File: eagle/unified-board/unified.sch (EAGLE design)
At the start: 78 parts, among them IC101 THAT151x, J103 phantom, J104 eqout, J601 out2, U101 OPAMPLME49710, U602 LM3915N, U603 OPAMPLME49710

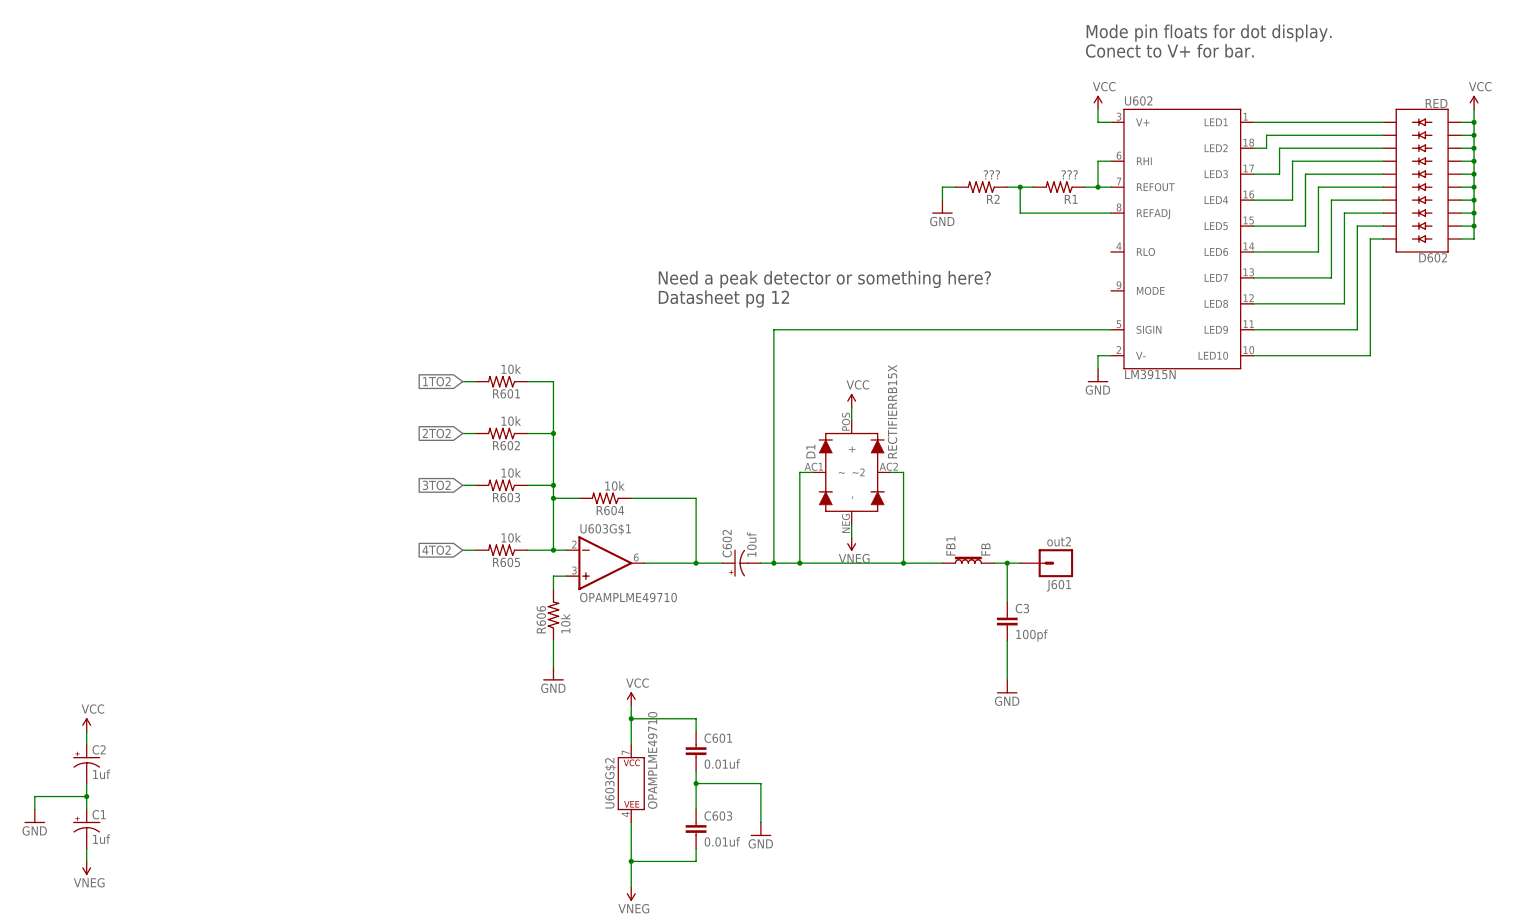
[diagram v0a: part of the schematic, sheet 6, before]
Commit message: Some initial routing
one input, one output, placeholders  for more.
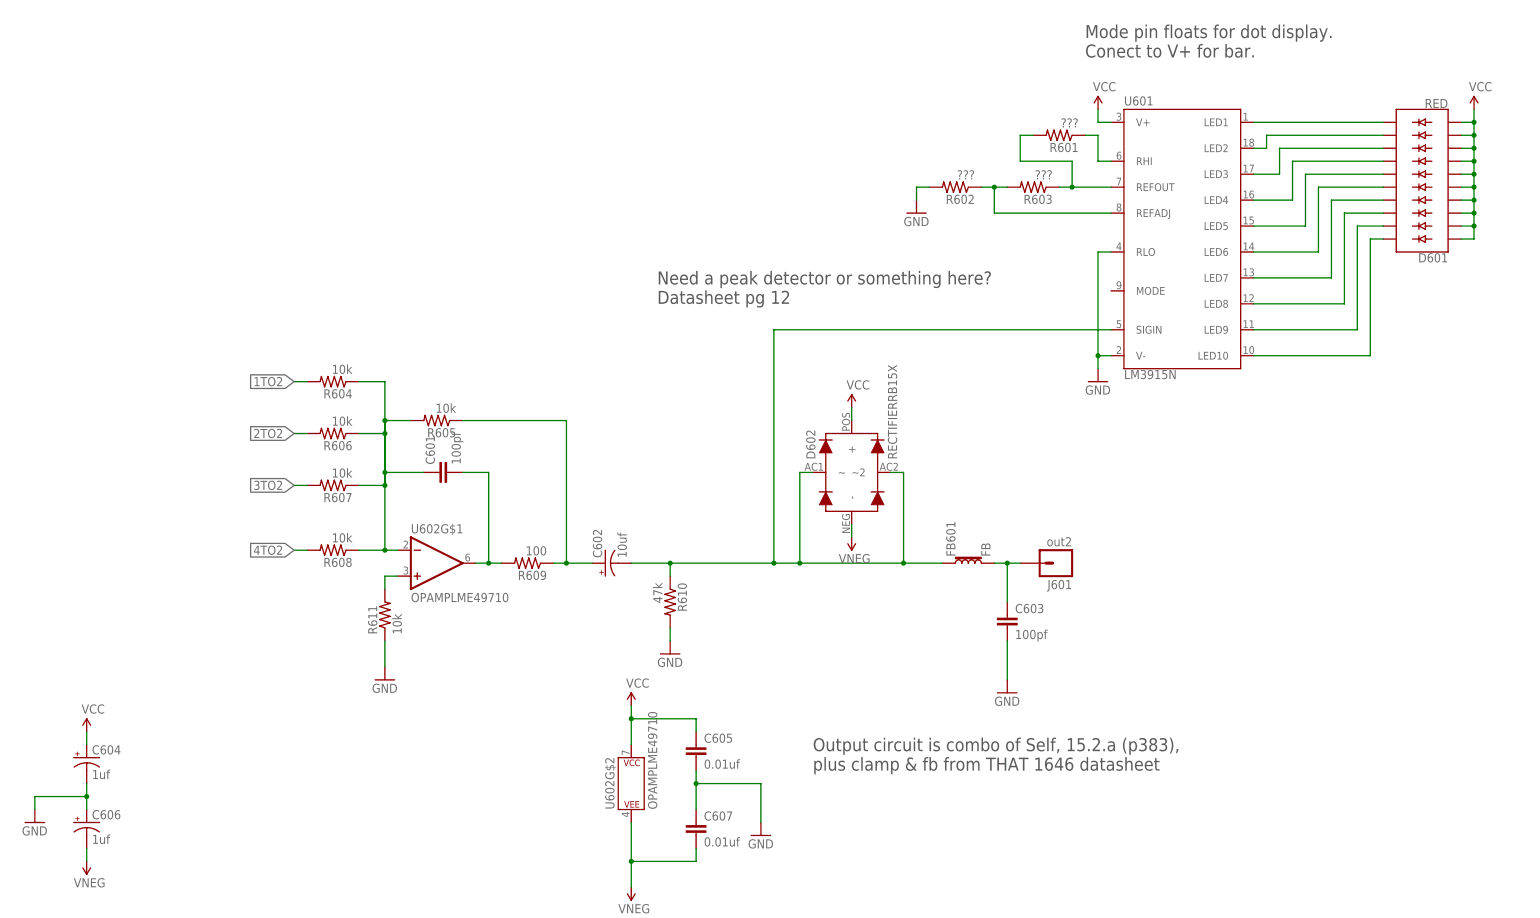
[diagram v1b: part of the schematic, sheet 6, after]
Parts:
- removed C3: 100pf, SparkFun-Capacitors:CAPPTH
- removed D1: RECTIFIERRB15X, mixer:RECTIFIERRB15X
- removed R1, R2: ???, SparkFun-Resistors:RESISTORAXIAL-0.3
- removed U603: OPAMPLME49710, mixer:OPAMPLME49710
- added C605, C607: 0.01uf, mixer:WIMA-MKS20.01UF
- added D601: RED, SparkFun-LED:LED_BARGRAPH_10RED
- added R607, R608, R611: 10k, SparkFun-Resistors:RESISTORAXIAL-0.3
- added R609: 100, SparkFun-Resistors:RESISTORAXIAL-0.3
- added R610: 47k, SparkFun-Resistors:RESISTORAXIAL-0.3
- added U601: LM3915N, SparkFun-IC-Special-Function:LM3915N
- C101, C102: value 47p -> 0.01uf; device SparkFun-Capacitors:CAPPTH -> mixer:WIMA-MKS20.01UF
- C103: value 470p -> 0.015uf; device SparkFun-Capacitors:CAPPTH -> mixer:WIMA-MKS20.015UF
- C104, C113: value 470p -> 0.1uf; device SparkFun-Capacitors:CAPPTH -> mixer:WIMA-MKS20.1UF
- C105: value 470p -> 22u; device SparkFun-Capacitors:CAPPTH -> SparkFun-Capacitors:100UF-25V-20%(PTH)
- C107: value 22u -> 470p; device SparkFun-Capacitors:100UF-25V-20%(PTH) -> SparkFun-Capacitors:CAPPTH
- C108, C120: value 22u -> 47p; device SparkFun-Capacitors:100UF-25V-20%(PTH) -> SparkFun-Capacitors:CAPPTH
- C110: value 22u -> 100pf; device SparkFun-Capacitors:100UF-25V-20%(PTH) -> SparkFun-Capacitors:CAPPTH
- C111: value 22u -> 0.015uf; device SparkFun-Capacitors:100UF-25V-20%(PTH) -> mixer:WIMA-MKS20.015UF
- C115: value 0.1uf -> 22u; device mixer:WIMA-MKS20.1UF -> SparkFun-Capacitors:100UF-25V-20%(PTH)
- C116: value 0.1uf -> 470p; device mixer:WIMA-MKS20.1UF -> SparkFun-Capacitors:CAPPTH
- C117, C118: value 0.015uf -> 22u; device mixer:WIMA-MKS20.015UF -> SparkFun-Capacitors:100UF-25V-20%(PTH)
- C119: value 100pf -> 470p
- C121: value 0.01uf -> 470p; device mixer:WIMA-MKS20.01UF -> SparkFun-Capacitors:CAPPTH
- C122: value 0.01uf -> 22u; device mixer:WIMA-MKS20.01UF -> SparkFun-Capacitors:100UF-25V-20%(PTH)
- C601, C603: value 0.01uf -> 100pf; device mixer:WIMA-MKS20.01UF -> SparkFun-Capacitors:CAPPTH
- D602: value RED -> RECTIFIERRB15X; device SparkFun-LED:LED_BARGRAPH_10RED -> mixer:RECTIFIERRB15X
- J101: value (none) -> phantom; device SparkFun-Connectors:M031X03_NO_SILK -> SparkFun-Connectors:M01NOSILK-KIT
- J103: value phantom -> eqout
- J104: value eqout -> (none); device SparkFun-Connectors:M01NOSILK-KIT -> SparkFun-Connectors:M031X03_NO_SILK
- R101: value 6k8 -> 1k8
- R102: value 6k8 -> 1k
- R103: value 10 -> 6k8
- R105: value 4k99 -> 1k
- R106: value 4k99 -> 1k2
- R107: value 22k -> 12k
- R108: value 1k2 -> 6k8
- R111: value 1k8 -> 10
- R113: value 12k -> 1k
- R114: value 1k -> 22k
- R115, R116: value 1k -> 4k99
- R601, R602, R603: value 10k -> ???
- U602: value LM3915N -> OPAMPLME49710; device SparkFun-IC-Special-Function:LM3915N -> mixer:OPAMPLME49710
- VR101: device mixer:POTROT-SW-POT -> mixer:POT10K-VERTPIN
- VR103: device mixer:POT10K-VERTPIN -> mixer:POTROT-SW-POT
- renumbered C1 to C606, C2 to C604, FB1 to FB601
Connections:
- new net N$12: C602.+, R605.1, R609.1
- new net N$53: R601.1, U601.RHI
- net 1TO2: now also R604.2; no longer R601.2
- net 2TO2: now also R606.2; no longer R602.2
- net 3TO2: now also R607.2; no longer R603.2
- net 4TO2: now also R608.2; no longer R605.2
- net GND: now also C101.2, C102.1, C106.2, C116.2, C603.2, C605.2, C607.1, R114.2, R602.2, R610.2, R611.1, U601.RLO, U601.V-; no longer C112.2, C113.2, C121.2, C122.1, C3.2, C601.2, C603.1, R107.2, R2.2, R606.1, U602.V-
- net N$1: now also C104.1, R101.1; no longer C115.1, R111.1
- net N$10: now also C111.1, VR101.E; no longer C118.1, VR103.E
- net N$11: now also D602.~, D602.~2, R610.1, U601.SIGIN; no longer D1.~, D1.~2, U602.SIGIN
- net N$13: now also R611.2, U602G$1.+IN; no longer R606.2, U603G$1.+IN
- net N$14: now also C104.2, C113.2, R107.2; no longer C115.2, C116.2, R113.2
- net N$15: now also C103.2, VR101.A; no longer C117.2, VR103.A
- net N$16: now also C601.2, R609.2, U602G$1.OUT; no longer C602.+, R604.1, U603G$1.OUT
- net N$17: now also C601.1, R604.1, R605.2, R606.1, R607.1, R608.1, U602G$1.-IN; no longer R601.1, R602.1, R603.1, R604.2, R605.1, U603G$1.-IN
- net N$19: now also C103.1, R102.1; no longer C117.1, R115.1
- net N$2: now also C113.1; no longer C116.1
- net N$20: now also D601.C9, U601.LED1; no longer D602.C9, U602.LED1
- net N$21: now also C115.-; no longer C111.-
- net N$22: now also C109.+; no longer C114.+
- net N$23: now also C108.1, J102.2; no longer C101.1, J101.2
- net N$24: now also C107.2, C108.2, C112.1; no longer C101.2, C103.2, C104.1
- net N$25: now also C105.+, C107.1, J102.3, R103.1; no longer C103.1, C107.+, J101.3, R101.1
- net N$26: now also C112.2, C114.+, J102.1, R108.1; no longer C104.2, C108.+, J101.1, R102.1
- net N$27: now also C114.-, R111.2; no longer C108.-, R104.2
- net N$28: now also J101.1, R103.2, R108.2; no longer J103.1, R101.2, R102.2
- net N$29: now also C105.-, R104.2; no longer C107.-, R103.2
- net N$3: now also C110.1, R105.2, R107.1; no longer C119.1, R113.1, R114.2
- net N$30: now also R104.1, R106.1, R115.1; no longer R103.1, R105.1, R108.1
- net N$31: now also R111.1, R116.1; no longer R104.1, R106.1
- net N$32: now also R106.2, R114.1; no longer R107.1, R108.2
- net N$33: now also VR103.A, VR103.S; no longer VR101.A, VR101.S
- net N$34: now also VR103.E; no longer VR101.E
- net N$35: now also C115.+; no longer C111.+
- net N$36: now also C120.1, J104.2; no longer C102.1, J102.2
- net N$37: now also C119.2, C120.2, C121.1; no longer C102.2, C105.2, C106.1
- net N$38: now also C117.+, C119.1, J104.3; no longer C105.1, C109.+, J102.3
- net N$39: now also C121.2, C122.+, J104.1; no longer C106.2, C110.+, J102.1
- net N$4: now also C111.2, R113.2; no longer C118.2, R116.2
- net N$40: now also C122.-, R116.2; no longer C110.-, R106.2
- net N$41: now also D601.C8, U601.LED2; no longer D602.C8, U602.LED2
- net N$42: now also C117.-, R115.2; no longer C109.-, R105.2
- net N$43: now also D601.C7, U601.LED3; no longer D602.C7, U602.LED3
- net N$44: now also D601.C6, U601.LED4; no longer D602.C6, U602.LED4
- net N$45: now also D601.C5, U601.LED5; no longer D602.C5, U602.LED5
- net N$46: now also D601.C4, U601.LED6; no longer D602.C4, U602.LED6
- net N$47: now also D601.C3, U601.LED7; no longer D602.C3, U602.LED7
- net N$48: now also D601.C2, U601.LED8; no longer D602.C2, U602.LED8
- net N$49: now also D601.C1, U601.LED9; no longer D602.C1, U602.LED9
- net N$5: now also C118.-, J103.1; no longer C120.-, J104.1
- net N$50: now also D601.C, U601.LED10; no longer D602.C, U602.LED10
- net N$51: now also R601.2, R603.1, U601.REFOUT; no longer R1.1, U602.REFOUT, U602.RHI
- net N$52: now also R602.1, R603.2, U601.REFADJ; no longer R1.2, R2.1, U602.REFADJ
- net N$6: now also C110.2, C118.+, R101.2, R102.2; no longer C119.2, C120.+, R111.2, R115.2
- net N$7: now also C603.1; no longer C3.1
- net N$8: now also R105.1, VR101.S; no longer R114.1, VR103.S
- net N$9: now also C109.-, R113.1; no longer C114.-, R116.1
- net VCC: now also C101.1, C106.1, C605.1, D601.A, D601.A1, D601.A2, D601.A3, D601.A4, D601.A5, D601.A6, D601.A7, D601.A8, D601.A9, D602.+, U601.V+, U602G$2.P$V+; no longer C112.1, C121.1, C601.1, D1.+, D602.A, D602.A1, D602.A2, D602.A3, D602.A4, D602.A5, D602.A6, D602.A7, D602.A8, D602.A9, U602.V+, U603G$2.P$V+
- net VNEG: now also C102.2, C116.1, C607.2, D602.-, U602G$2.P$V-; no longer C113.1, C122.2, C603.2, D1.-, U603G$2.P$V-
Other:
- note added: "Output circuit is combo of Self, 15.2.a (p383), plus clamp & fb from THAT 1646 datasheet"
- moved on the sheet: C101, C102, C103, C104, C106, C109, C112, C113, C114, C116, C119, C121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

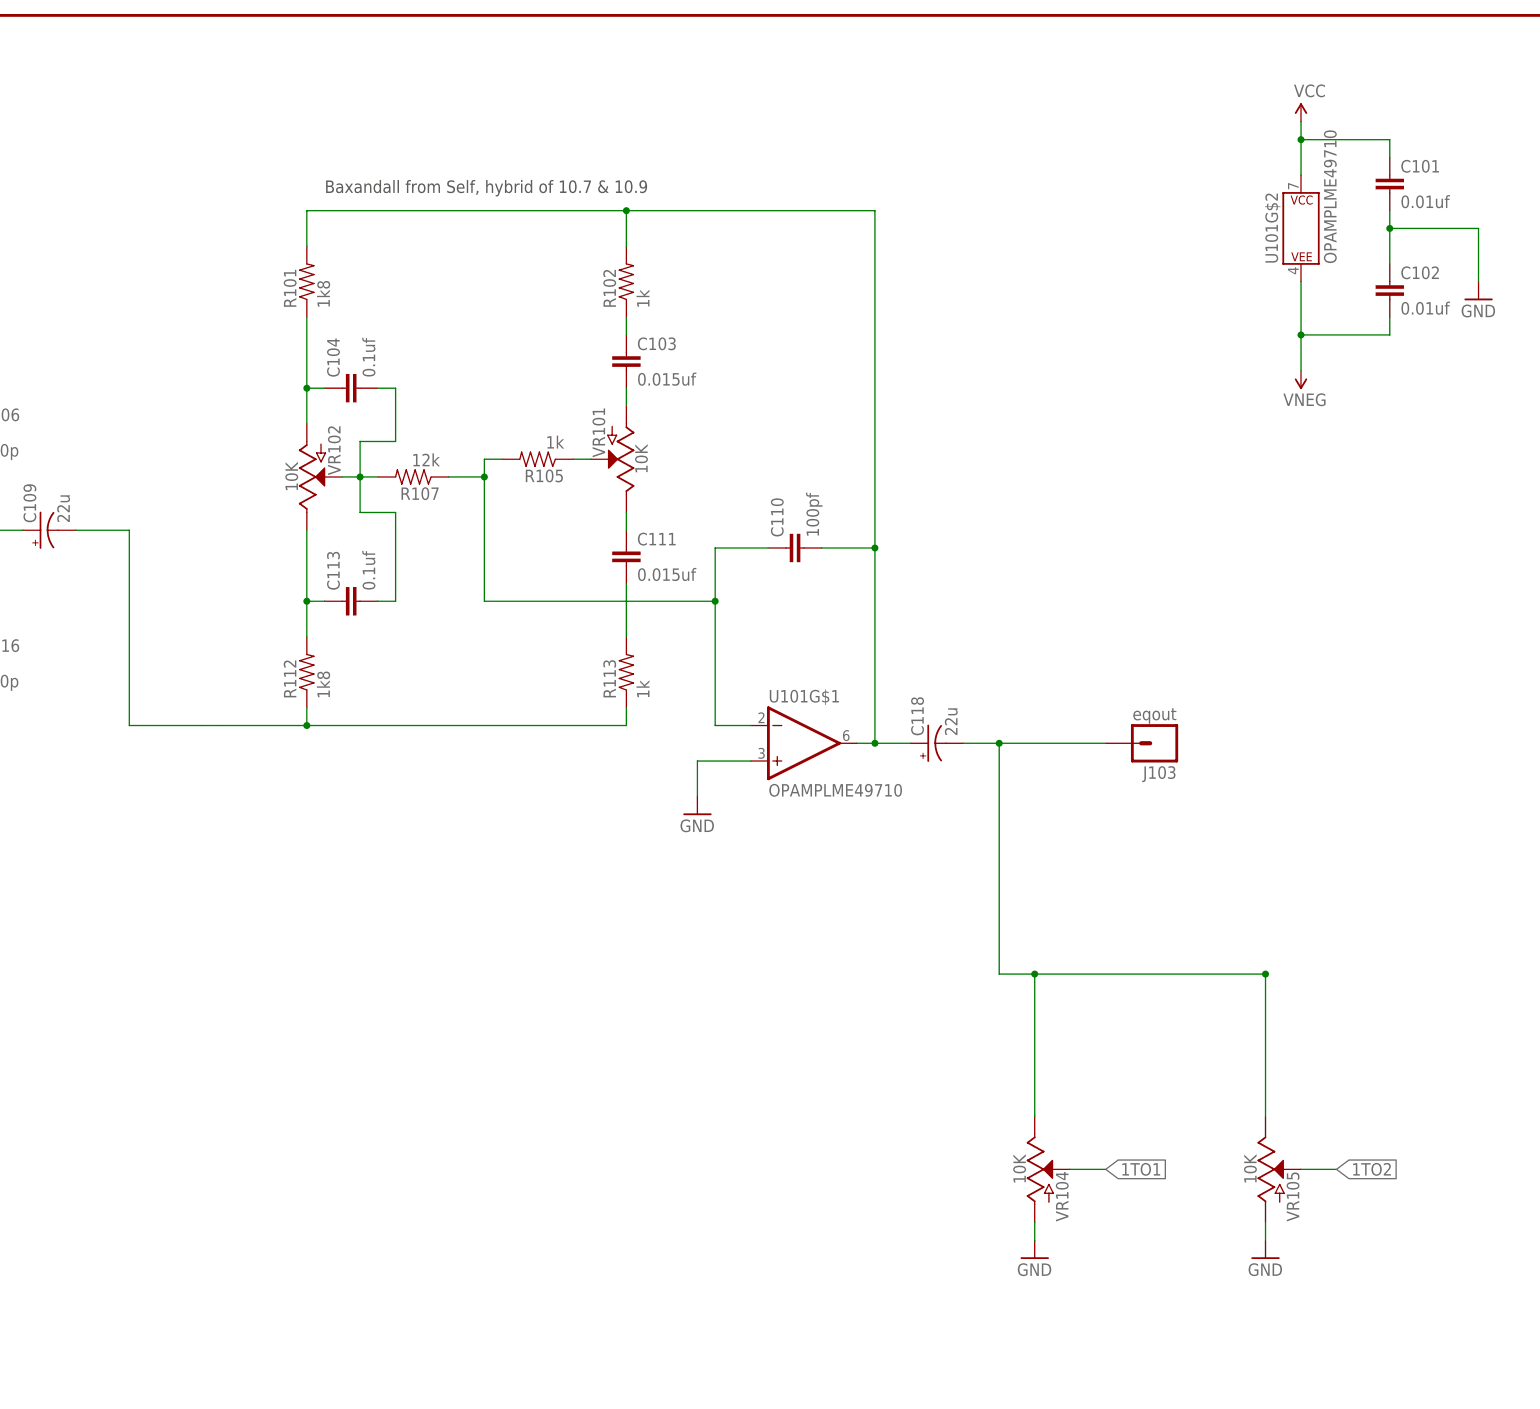
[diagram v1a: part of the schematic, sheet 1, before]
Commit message: A few tweaks.
Forgot that it needs to run right-to-left.
Added standoffs and some silk legending.
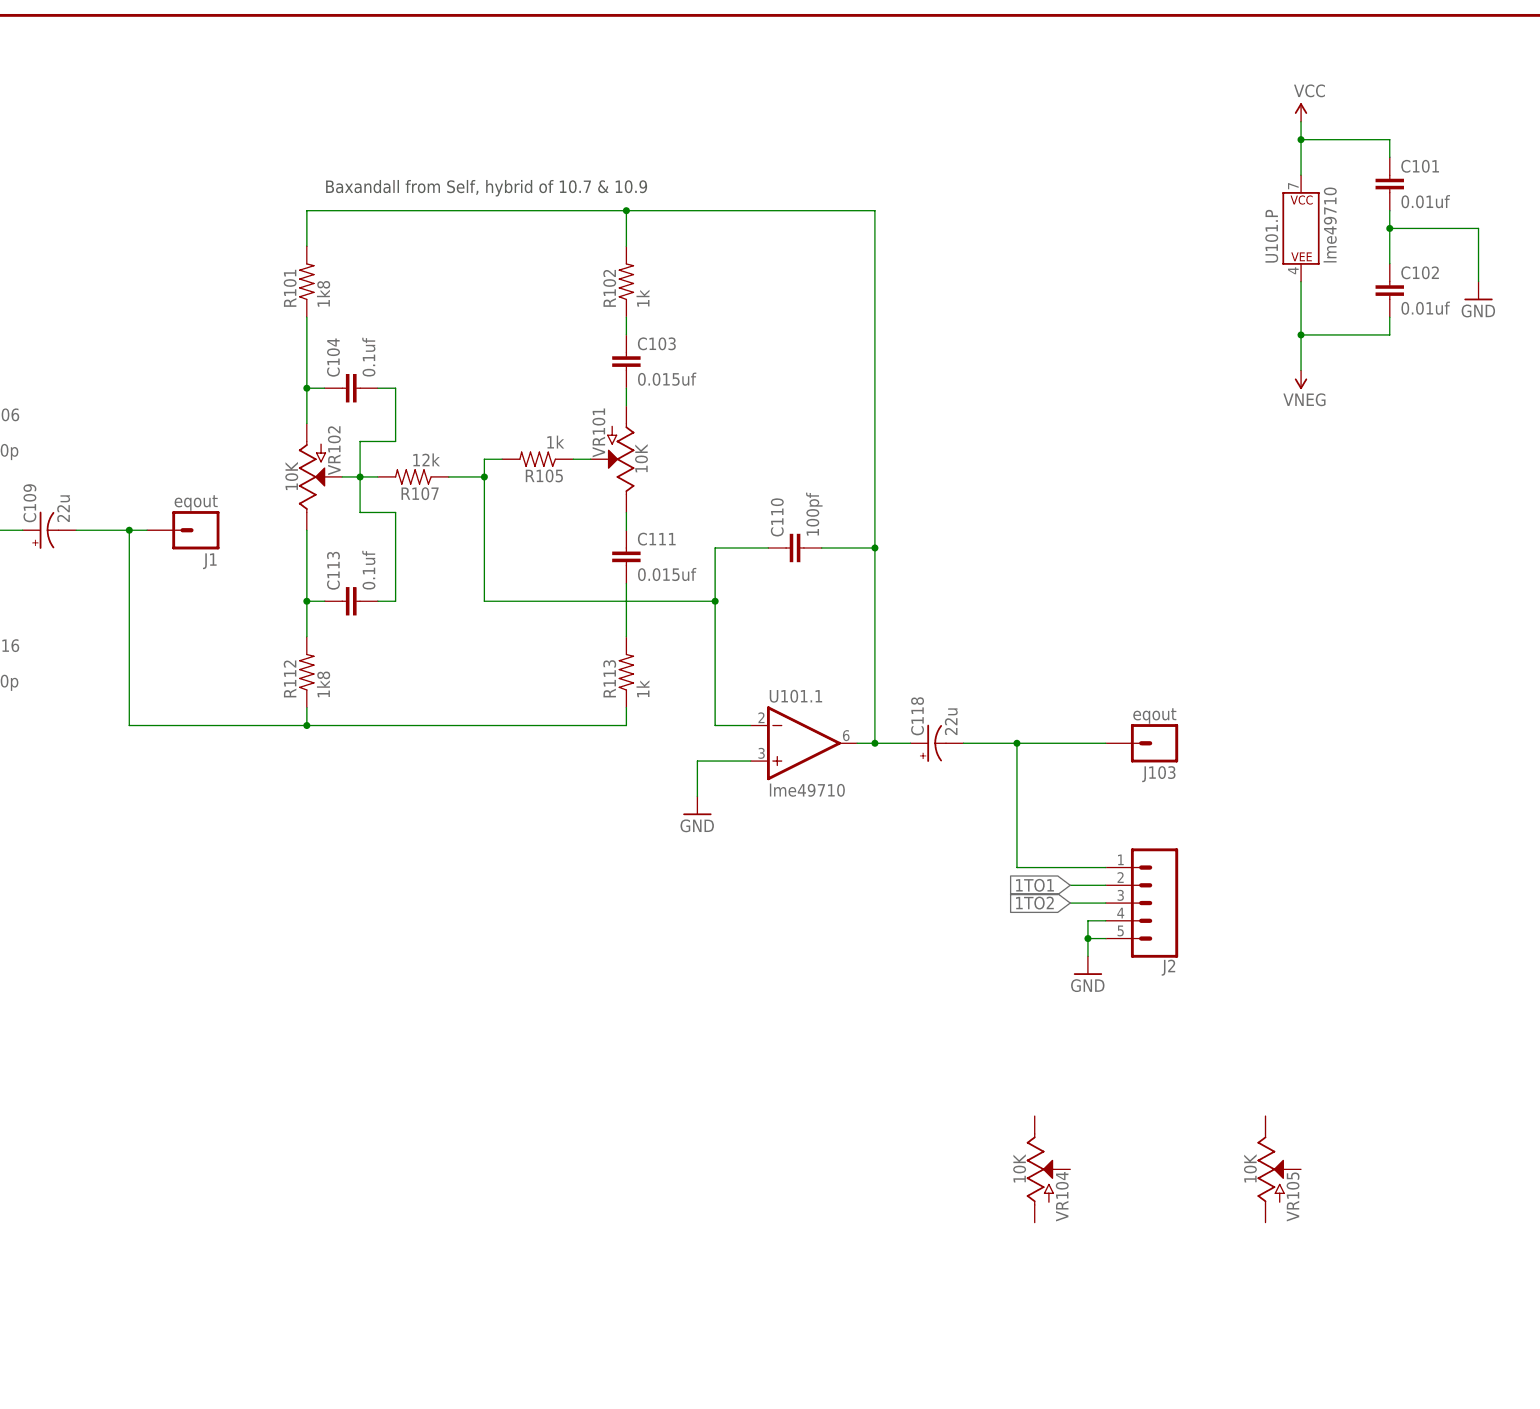
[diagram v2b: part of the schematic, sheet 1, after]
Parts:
- added H1, H10, H11, H12, H2, H3, H4, H5, H6, H7, H8, H9: STAND-OFF, SparkFun-Hardware:STAND-OFF
- added J1: eqout, SparkFun-Connectors:M01NOSILK-KIT
- added J2: (no value), SparkFun-Connectors:CONN_05PTH_LONGPADS
- J601: device SparkFun-Connectors:M01NOSILK-KIT -> SparkFun-Connectors:CONN_02LOCK_LONGPADS
- U101, U602: value OPAMPLME49710 -> lme49710
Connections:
- removed net N$5: C118.-, J103.1, VR104.E, VR105.E
- new net EQ1OUT: C118.-, J103.1, J2.1
- net 1TO1: now also J2.2; no longer VR104.S
- net 1TO2: now also J2.3; no longer VR105.S
- net GND: now also J2.4, J2.5, J601.2, U101.1.+IN; no longer U101G$1.+IN, VR104.A, VR105.A
- net N$13: now also U602.1.+IN; no longer U602G$1.+IN
- net N$16: now also U602.1.OUT; no longer U602G$1.OUT
- net N$17: now also U602.1.-IN; no longer U602G$1.-IN
- net N$3: now also U101.1.-IN; no longer U101G$1.-IN
- net N$6: now also U101.1.OUT; no longer U101G$1.OUT
- net N$9: now also J1.1
- net VCC: now also U101.P.P$V+, U602.P.P$V+; no longer U101G$2.P$V+, U602G$2.P$V+
- net VNEG: now also U101.P.P$V-, U602.P.P$V-; no longer U101G$2.P$V-, U602G$2.P$V-
